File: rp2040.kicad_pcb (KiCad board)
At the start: 2 copper layers, 32 parts, among them J1 USB_C_Receptacle_USB2.0, J2 Conn_01x18, J3 Conn_01x18, SW1 SW_SPST, SW2 SW_SPST, U1 W25Q32JVSS, U2 AP1117-33, U3 RP2040, Y1 12MHz

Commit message: Routing finished
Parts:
- added J4: Conn_01x08, footprints:SOIC_clipProgSmall, F.Cu at (144.8, 104.5)
- added R8: 1K, Resistor_SMD:R_0402_1005Metric_Pad0.72x0.64mm_HandSolder, F.Cu at (168.9, 95.8)
- added kibuzzard-6203A46A: G***, kibuzzard-6203A46A, F.Cu at (178.1, 86.2)
- added kibuzzard-6203A47E: G***, kibuzzard-6203A47E, F.Cu at (178.1, 103.8)
- C1, C10, C11, C12, C13, C14, C15, C16, C4, C5, C6, C7, C8, C9: footprint Capacitor_SMD:C_0603_1608Metric_Pad1.08x0.95mm_HandSolder -> Capacitor_SMD:C_0402_1005Metric_Pad0.74x0.62mm_HandSolder
- C2, C3, U2: moved to B.Cu
- J2, J3: value Conn_01x18 -> Conn_02x10_Odd_Even; footprint Connector_PinHeader_2.54mm:PinHeader_1x18_P2.54mm_Vertical -> Connector_PinHeader_2.54mm:PinHeader_2x10_P2.54mm_Vertical
- R1, R2, R3, R4, R5, R6, R7: footprint Resistor_SMD:R_0603_1608Metric_Pad0.98x0.95mm_HandSolder -> Resistor_SMD:R_0402_1005Metric_Pad0.72x0.64mm_HandSolder
- U1: footprint Package_SO:SOIC-8_5.23x5.23mm_P1.27mm -> USON:SOIC-USON-8
- moved SW2 67.6 mm to (179.6, 108.5)
- moved R5 65.4 mm to (181.1, 105.5)
- moved C4 58.5 mm to (172.2, 99.0), turned to 180 degrees
- moved C13 56.1 mm to (164.3, 101.8), turned to -90 degrees
- moved C9 53.8 mm to (155.9, 95.7), turned to 180 degrees
- moved R7 53.4 mm to (156.6, 93.7), turned to 180 degrees
- moved R4 53.2 mm to (180.8, 89.3)
- moved U2 51.8 mm to (171.6, 89.5), turned to 180 degrees
- moved R6 51.8 mm to (156.6, 94.7), turned to 180 degrees
- moved C2 50.7 mm to (174.3, 94.0), turned to 180 degrees
- moved C11 50.7 mm to (159.8, 101.4), turned to -90 degrees
- moved C7 50.5 mm to (170.0, 92.5)
- moved Y1 50.3 mm to (172.2, 96.8), turned to 180 degrees
- moved C1 48.4 mm to (146.7, 89.4)
- moved R3 47.8 mm to (180.8, 101.2), turned to 180 degrees
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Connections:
- J2 pad 10: /GPIO8 -> /GPIO7
- J2 pad 11: /GPIO9 -> /GPIO8
- J2 pad 12: /GPIO10 -> /GPIO9
- J2 pad 13: /GPIO11 -> /GPIO10
- J2 pad 14: /GPIO12 -> /GPIO11
- J2 pad 15: /GPIO13 -> /GPIO12
- J2 pad 16: /GPIO14 -> +3V3
- J2 pad 17: /GPIO15 -> /GPIO13
- J2 pad 18: GND -> /GPIO14
- J2 pad 2: /GPIO0 -> /RUN
- J2 pad 3: /GPIO1 -> unconnected-(J2-Pad3)
- J2 pad 4: /GPIO2 -> unconnected-(J2-Pad4)
- J2 pad 5: /GPIO3 -> /GPIO2
- J2 pad 6: /GPIO4 -> /GPIO3
- J2 pad 7: /GPIO5 -> /GPIO4
- J2 pad 8: /GPIO6 -> /GPIO5
- J2 pad 9: /GPIO7 -> /GPIO6
- J3 pad 1: GND -> /GPIO0
- J3 pad 10: /GPIO22 -> /GPIO25
- J3 pad 11: /GPIO23 -> /GPIO22
- J3 pad 12: /GPIO24 -> /GPIO23
- J3 pad 13: /GPIO25 -> GND
- J3 pad 14: /GPIO26 -> /GPIO21
- J3 pad 15: /GPIO27 -> VBUS
- J3 pad 16: /GPIO28 -> /GPIO20
- J3 pad 17: /GPIO29 -> /GPIO18
- J3 pad 18: GND -> /GPIO19
- J3 pad 2: VBUS -> GND
- J3 pad 3: +3V3 -> /GPIO1
- J3 pad 4: /GPIO16 -> unconnected-(J3-Pad4)
- J3 pad 5: /GPIO17 -> /GPIO28
- J3 pad 6: /GPIO18 -> /GPIO29
- J3 pad 7: /GPIO19 -> /GPIO26
- J3 pad 8: /GPIO20 -> /GPIO27
- J3 pad 9: /GPIO21 -> /GPIO24
- R5 pad 2: Net-(R5-Pad2) -> /RUN
- SW2 pad 2: Net-(R5-Pad2) -> /RUN
- U3 pad 21: Net-(C5-Pad2) -> Net-(R8-Pad2)
- U3 pad 24: unconnected-(U3-Pad24) -> /SWCLK
- U3 pad 25: unconnected-(U3-Pad25) -> /SWD
- U3 pad 26: Net-(R5-Pad2) -> /RUN
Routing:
- net +3V3: track 0.00 -> 124.0 mm, vias 0 -> 8
- net /QSPI_SS: track 0.00 -> 71.0 mm, vias 0 -> 2
- net /RUN: track 0.00 -> 67.5 mm, vias 0 -> 2
- net /GPIO1: track 0.00 -> 41.8 mm, vias 0 -> 2
- net /USB_D+: track 0.00 -> 39.5 mm, vias 0 -> 2
- net /USB_D-: track 0.00 -> 37.7 mm, vias 0 -> 2
- net /GPIO0: track 0.00 -> 35.7 mm, vias 0 -> 2
- net /SWCLK: track 0.00 -> 29.2 mm, vias 0 -> 1
- net /SWD: track 0.00 -> 27.7 mm, vias 0 -> 1
- net VBUS: track 0.00 -> 25.4 mm, vias 0 -> 2
- net /QSPI_SD3: track 0.00 -> 23.2 mm
- net /QSPI_SCLK: track 0.00 -> 21.7 mm
- net +1V1: track 0.00 -> 21.2 mm
- net /QSPI_SDO: track 0.00 -> 20.4 mm
- net /QSPI_SD1: track 0.00 -> 18.1 mm
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- added copper zone on B.Cu, net GND
- added copper zone on F.Cu, net GND
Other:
- board outline added: 39 x 31 mm

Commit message: Some random tweaks
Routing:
- net /GPIO2: track 16.6 -> 16.0 mm
- net /GPIO4: track 14.5 -> 13.9 mm
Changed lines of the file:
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@@
   (segment (start 150.4 102) (end 152.45 102) (width 0.2) (layer "B.Cu") (net 13))
   (segment (start 161.15 100.35) (end 161.35 100.15) (width 0.2) (layer "B.Cu") (net 13))
-  (segment (start 161.801467 102.098533) (end 160.7 103.2) (width 0.2) (layer "F.Cu") (net 14))
-  (segment (start 156.25 103.2) (end 154.85 104.6) (width 0.2) (layer "F.Cu") (net 14))
+  (segment (start 156 104.6) (end 154.85 105.75) (width 0.2) (layer "F.Cu") (net 14))
+  (segment (start 161.802444 100.141843) (end 161.802445 100.191839) (width 0.2) (layer "F.Cu") (net 14))
+  (segment (start 161.802445 100.191839) (end 161.801467 100.192817) (width 0.2) (layer "F.Cu") (net 14))
   (segment (start 161.801467 100.19303) (end 161.801319 100.193178) (width 0.2) (layer "F.Cu") (net 14))
-  (segment (start 161.802445 100.191839) (end 161.801467 100.192817) (width 0.2) (layer "F.Cu") (net 14))
-  (segment (start 161.801467 100.192817) (end 161.801467 100.19303) (width 0.2) (layer "F.Cu") (net 14))
+  (segment (start 159.3 104.6) (end 156 104.6) (width 0.2) (layer "F.Cu") (net 14))
+  (segment (start 161.801319 100.193178) (end 161.801467 100.33795) (width 0.2) (layer "F.Cu") (net 14))
   (segment (start 161.9 98.6875) (end 161.849511 98.737989) (width 0.2) (layer "F.Cu") (net 14))
-  (segment (start 161.802444 100.141843) (end 161.802445 100.191839) (width 0.2) (layer "F.Cu") (net 14))
-  (segment (start 160.7 103.2) (end 156.25 103.2) (width 0.2) (layer "F.Cu") (net 14))
-  (segment (start 154.85 104.6) (end 154.85 107.86) (width 0.2) (layer "F.Cu") (net 14))
   (segment (start 161.801467 100.33795) (end 161.801467 102.098533) (width 0.2) (layer "F.Cu") (net 14))
-  (segment (start 161.801319 100.193178) (end 161.801467 100.33795) (width 0.2) (layer "F.Cu") (net 14))
   (segment (start 154.85 107.86) (end 156.215 109.225) (width 0.2) (layer "F.Cu") (net 14))
   (segment (start 161.849511 98.737989) (end 161.849511 100.094776) (width 0.2) (layer "F.Cu") (net 14))
+  (segment (start 154.85 105.75) (end 154.85 107.86) (width 0.2) (layer "F.Cu") (net 14))
+  (segment (start 161.801467 102.098533) (end 159.3 104.6) (width 0.2) (layer "F.Cu") (net 14))
+  (segment (start 161.801467 100.192817) (end 161.801467 100.19303) (width 0.2) (layer "F.Cu") (net 14))
   (segment (start 161.849511 100.094776) (end 161.802444 100.141843) (width 0.2) (layer "F.Cu") (net 14))
-  (segment (start 157.38 103.7) (end 156.215 104.865) (width 0.2) (layer "F.Cu") (net 15))
+  (segment (start 156.215 105.685) (end 156.215 106.685) (width 0.2) (layer "F.Cu") (net 15))
+  (segment (start 162.150978 102.249022) (end 159.45 104.95) (width 0.2) (layer "F.Cu") (net 15))
+  (segment (start 162.3 98.6875) (end 162.3 100.188571) (width 0.2) (layer "F.Cu") (net 15))
   (segment (start 162.3 100.188571) (end 162.150978 100.337593) (width 0.2) (layer "F.Cu") (net 15))
-  (segment (start 162.150978 102.249022) (end 160.7 103.7) (width 0.2) (layer "F.Cu") (net 15))
-  (segment (start 156.215 104.865) (end 156.215 106.685) (width 0.2) (layer "F.Cu") (net 15))
-  (segment (start 160.7 103.7) (end 157.38 103.7) (width 0.2) (layer "F.Cu") (net 15))
+  (segment (start 159.45 104.95) (end 156.95 104.95) (width 0.2) (layer "F.Cu") (net 15))
   (segment (start 162.150978 100.337593) (end 162.150978 102.249022) (width 0.2) (layer "F.Cu") (net 15))
-  (segment (start 162.3 98.6875) (end 162.3 100.188571) (width 0.2) (layer "F.Cu") (net 15))
-  (segment (start 157.655489 104.794511) (end 158.25 104.2) (width 0.2) (layer "F.Cu") (net 16))
-  (segment (start 162.649511 100.333343) (end 162.649511 99.717642) (width 0.2) (layer "F.Cu") (net 16))
-  (segment (start 162.649511 99.717642) (end 162.7 99.667153) (width 0.2) (layer "F.Cu") (net 16))
-  (segment (start 157.655489 108.125489) (end 157.655489 104.794511) (width 0.2) (layer "F.Cu") (net 16))
-  (segment (start 162.500489 100.482365) (end 162.649511 100.333343) (width 0.2) (layer "F.Cu") (net 16))
-  (segment (start 158.755 109.225) (end 157.655489 108.125489) (width 0.2) (layer "F.Cu") (net 16))
-  (segment (start 162.500489 102.449511) (end 162.500489 100.482365) (width 0.2) (layer "F.Cu") (net 16))
-  (segment (start 162.7 99.667153) (end 162.7 98.6875) (width 0.2) (layer "F.Cu") (net 16))
-  (segment (start 158.25 104.2) (end 160.75 104.2) (width 0.2) (layer "F.Cu") (net 16))
-  (segment (start 160.75 104.2) (end 162.500489 102.449511) (width 0.2) (layer "F.Cu") (net 16))
+  (segment (start 156.95 104.95) (end 156.215 105.685) (width 0.2) (layer "F.Cu") (net 15))
+  (segment (start 162.500489 100.482365) (end 162.500489 102.449511) (width 0.2) (layer "F.Cu") (net 16))
+  (segment (start 162.7 98.6875) (end 162.7 99.667153) (width 0.2) (layer "F.Cu") (net 16))
+  (segment (start 162.500489 102.449511) (end 159.65 105.3) (width 0.2) (layer "F.Cu") (net 16))
+  (segment (start 157.6 106) (end 157.6 108.07) (width 0.2) (layer "F.Cu") (net 16))
+  (segment (start 162.7 99.667153) (end 162.649511 99.717642) (width 0.2) (layer "F.Cu") (net 16))
+  (segment (start 158.3 105.3) (end 157.6 106) (width 0.2) (layer "F.Cu") (net 16))
+  (segment (start 159.65 105.3) (end 158.3 105.3) (width 0.2) (layer "F.Cu") (net 16))
+  (segment (start 162.649511 99.717642) (end 162.649511 100.333343) (width 0.2) (layer "F.Cu") (net 16))
+  (segment (start 162.649511 100.333343) (end 162.500489 100.482365) (width 0.2) (layer "F.Cu") (net 16))
+  (segment (start 157.6 108.07) (end 158.755 109.225) (width 0.2) (layer "F.Cu") (net 16))
   (segment (start 162.850978 102.699022) (end 162.850978 100.62616) (width 0.2) (layer "F.Cu") (net 17))
   (segment (start 158.755 106.685) (end 158.865 106.685) (width 0.2) (layer "F.Cu") (net 17))

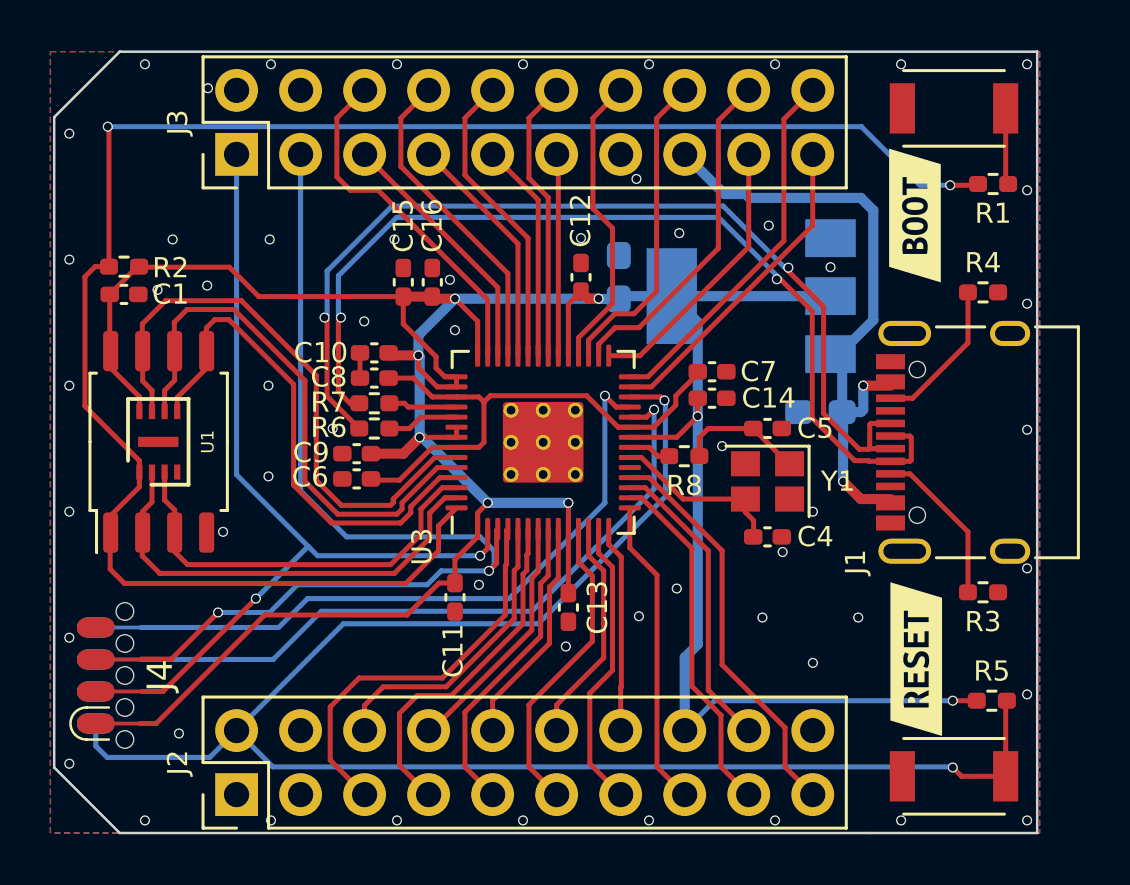
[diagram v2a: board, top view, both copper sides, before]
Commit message: Rearranged pinheaders, added logo and random tweaks
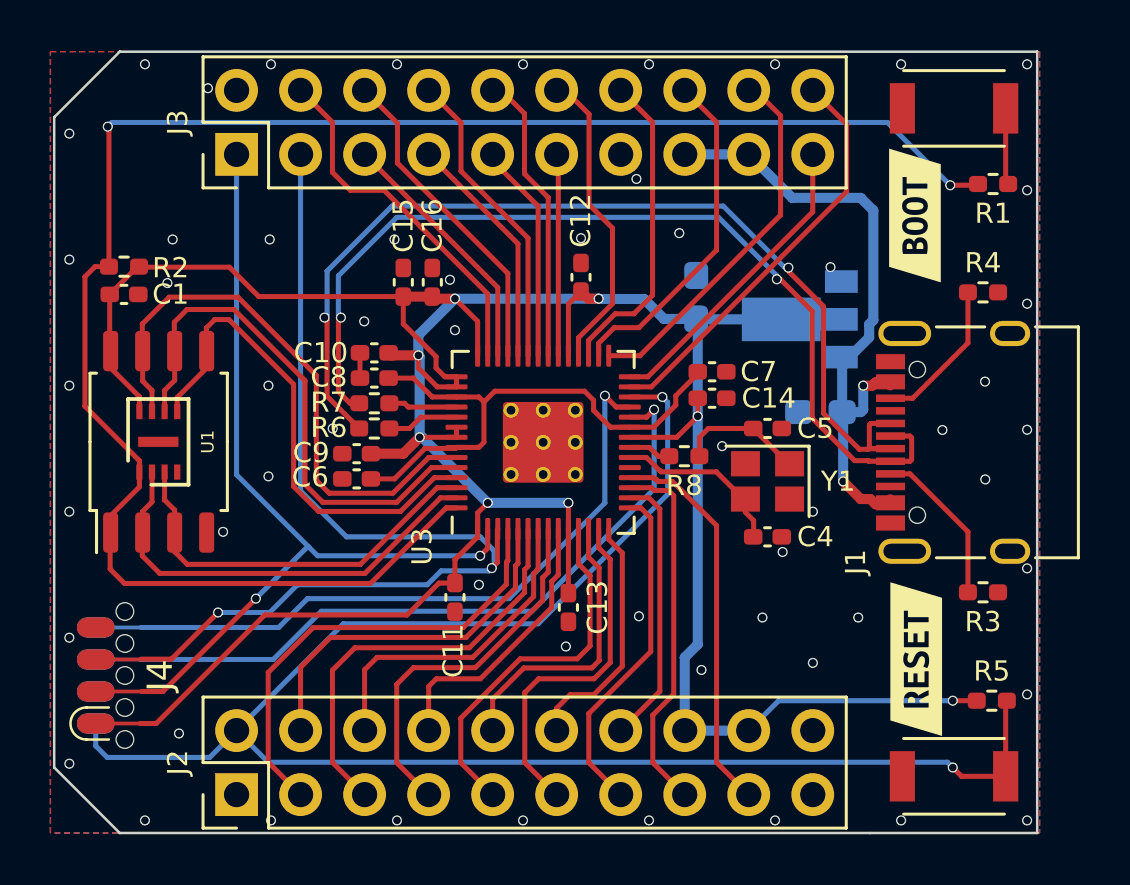
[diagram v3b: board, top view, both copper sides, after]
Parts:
- added G***: LOGO, LOGO, B.Cu at (154.1, 93.7)
- U2: footprint Package_TO_SOT_SMD:SOT-223-3_TabPin2 -> Package_TO_SOT_SMD:SOT-89-3
- moved C3 3.17 mm to (169.4, 89.5)
- moved U2 2.14 mm to (173.5, 90.4)
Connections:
- J2 pad 10: /GPIO7 -> /GPIO9
- J2 pad 11: /GPIO8 -> /GPIO10
- J2 pad 12: /GPIO9 -> /GPIO11
- J2 pad 13: /GPIO10 -> /GPIO12
- J2 pad 14: /GPIO11 -> /GPIO13
- J2 pad 15: /GPIO12 -> /GPIO14
- J2 pad 17: /GPIO13 -> /GPIO15
- J2 pad 18: /GPIO14 -> +3V3
- J2 pad 19: /GPIO15 -> GND
- J2 pad 20: unconnected-(J2-Pad20) -> GND
- J2 pad 3: unconnected-(J2-Pad3) -> /GPIO2
- J2 pad 4: unconnected-(J2-Pad4) -> /GPIO3
- J2 pad 5: /GPIO2 -> /GPIO4
- J2 pad 6: /GPIO3 -> /GPIO5
- J2 pad 7: /GPIO4 -> /GPIO6
- J2 pad 8: /GPIO5 -> /GPIO7
- J2 pad 9: /GPIO6 -> /GPIO8
- J3 pad 10: /GPIO25 -> /GPIO23
- J3 pad 12: /GPIO23 -> /GPIO21
- J3 pad 14: /GPIO21 -> /GPIO20
- J3 pad 16: /GPIO20 -> /GPIO19
- J3 pad 17: /GPIO18 -> VBUS
- J3 pad 18: /GPIO19 -> /GPIO18
- J3 pad 19: /GPIO16 -> /GPIO17
- J3 pad 20: /GPIO17 -> /GPIO16
- J3 pad 4: unconnected-(J3-Pad4) -> /GPIO29
- J3 pad 6: /GPIO29 -> /GPIO27
- J3 pad 8: /GPIO27 -> /GPIO25
- U1 pad 9: (no net) -> GND
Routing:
- net /GPIO18: track 11.0 -> 14.8 mm
- net /GPIO16: track 12.7 -> 16.4 mm
- net /GPIO5: track 9.86 -> 13.1 mm
- net /GPIO13: track 14.0 -> 10.8 mm
- net /GPIO4: track 13.9 -> 16.9 mm
- net /GPIO3: track 12.0 -> 14.7 mm
- net /GPIO14: track 11.9 -> 14.6 mm
- net /GPIO6: track 12.4 -> 15.0 mm
- net /GPIO17: track 14.8 -> 12.2 mm
- net /GPIO2: track 16.0 -> 18.5 mm
- net /GPIO9: track 9.02 -> 11.5 mm
- net /GPIO8: track 12.3 -> 14.7 mm
- net /GPIO10: track 11.6 -> 13.9 mm
- net /GPIO7: track 9.08 -> 11.2 mm
- net /GPIO11: track 8.21 -> 9.85 mm
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
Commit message: Final touches for the manufacturing process
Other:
- board text added: "JLCJLCJLCJLC"
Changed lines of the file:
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@@
       (usegerberattributes true)
       (usegerberadvancedattributes true)
-      (creategerberjobfile true)
+      (creategerberjobfile false)
       (svguseinch false)
       (svgprecision 6)
@@
     (property "Sheetname" "")
     (attr smd)
-    (fp_text reference "U3" (at -4.136575 -4.801255 90) (layer "F.SilkS")
+    (fp_text reference "U3" (at -3.43 -5.21 180) (layer "F.SilkS")
       (effects (font (size 0.8 0.8) (thickness 0.15)))
     )
@@
     (property "Sheetname" "")
     (attr smd)
-    (fp_text reference "C12" (at 2.25 -0.006137 90) (layer "F.SilkS")
+    (fp_text reference "C12" (at -0.01 -1.11 90) (layer "F.SilkS")
       (effects (font (size 0.8 0.8) (thickness 0.15)))
     )
@@
     (property "Sheetname" "")
     (attr smd)
-    (fp_text reference "C11" (at 2.12132 0.070711 90) (layer "F.SilkS")
+    (fp_text reference "C11" (at 0.01 -1.1 90) (layer "F.SilkS")
       (effects (font (size 0.8 0.8) (thickness 0.15)))
     )
@@
     (property "Sheetname" "")
     (attr smd)
-    (fp_text reference "J1" (at -4.75 -5.05 90) (layer "F.SilkS")
+    (fp_text reference "J1" (at -5.15 -5.16 180) (layer "F.SilkS")
       (effects (font (size 0.8 0.8) (thickness 0.15)))
     )
@@
     (attr smd)
     (fp_text reference "U1" (at 1.96 0 90) (layer "F.SilkS")
-      (effects (font (size 0.5 0.5) (thickness 0.125)))
+      (effects (font (size 0.8 0.8) (thickness 0.125)))
     )
     (fp_text value "W25Q32JVSS" (at 2.7232 0.035 90) (layer "F.Fab") hide
@@
     )
     (fp_text user "${REFERENCE}" (at 0.015 0 90) (layer "F.Fab")
-      (effects (font (size 1 1) (thickness 0.15)))
+      (effects (font (size 0.8 0.8) (thickness 0.15)))
     )
     (fp_line (start 2.74 -2.725) (end 2.48 -2.725) (layer "F.SilkS") (width 0.12))
@@
     (attr through_hole)
     (fp_text reference "J4" (at 0 -3.302 90) (layer "F.SilkS")
-      (effects (font (size 1 1) (thickness 0.15)))
+      (effects (font (size 0.8 0.8) (thickness 0.15)))
     )
     (fp_text value "Conn_01x08" (at 0.127 1.397 90) (layer "F.Fab")
@@
     (attr board_only exclude_from_pos_files exclude_from_bom)
     (fp_text reference "kibuzzard-6203A47E" (at 0 -1.025901 90) (layer "F.SilkS") hide
-      (effects (font (size 0.000254 0.000254) (thickness 0.000003)))
+      (effects (font (size 0.8 0.8) (thickness 0.000003)))
     )
     (fp_text value "G***" (at 0 1.025901 90) (layer "F.SilkS") hide
@@
     (property "Sheetname" "")
     (attr smd)
-    (fp_text reference "C16" (at 2.25 0 90) (layer "F.SilkS")
+    (fp_text reference "C16" (at 0 1.27 90) (layer "F.SilkS")
       (effects (font (size 0.8 0.8) (thickness 0.15)))
     )
@@
     (property "Sheetname" "")
     (attr smd)
-    (fp_text reference "C15" (at 2.25 0 90) (layer "F.SilkS")
+    (fp_text reference "C15" (at -0.01 -1.03 90) (layer "F.SilkS")
       (effects (font (size 0.8 0.8) (thickness 0.15)))
     )
@@
     (attr board_only exclude_from_pos_files exclude_from_bom)
     (fp_text reference "kibuzzard-6203A46A" (at 0 -1.025901 90) (layer "F.SilkS") hide
-      (effects (font (size 0.000254 0.000254) (thickness 0.000003)))
+      (effects (font (size 0.8 0.8) (thickness 0.000003)))
     )
     (fp_text value "G***" (at 0 1.025901 90) (layer "F.SilkS") hide
@@
     (property "Sheetname" "")
     (attr smd)
-    (fp_text reference "C3" (at 2.5 0 90) (layer "B.SilkS")
+    (fp_text reference "C3" (at -0.0075 -1.33 90) (layer "B.SilkS")
       (effects (font (size 0.8 0.8) (thickness 0.15)) (justify mirror))
     )
@@
     (property "Sheetname" "")
     (attr smd)
-    (fp_text reference "C2" (at 2.25 0) (layer "B.SilkS")
+    (fp_text reference "C2" (at 0.01 -1.54) (layer "B.SilkS")
       (effects (font (size 0.8 0.8) (thickness 0.15)) (justify mirror))
     )
@@
     (attr smd)
     (fp_text reference "U2" (at 0.3 3.5) (layer "B.SilkS")
-      (effects (font (size 1 1) (thickness 0.15)) (justify mirror))
+      (effects (font (size 0.8 0.8) (thickness 0.15)) (justify mirror))
     )
     (fp_text value "AP1117-33" (at 0.3 -3.5) (layer "B.Fab")
@@
     )
     (fp_text user "${REFERENCE}" (at 0.5 0 90) (layer "B.Fab")
-      (effects (font (size 1 1) (thickness 0.15)) (justify mirror))
+      (effects (font (size 0.8 0.8) (thickness 0.15)) (justify mirror))
     )
     (fp_line (start 1.66 -1.05) (end 1.66 -2.36) (layer "B.SilkS") (width 0.12))
@@
       (primitives
         (gr_poly (pts
+            (xy 3.8625 0.8665)
+            (xy 0.7375 0.8665)
+            (xy 0.7375 -0.8665)
             (xy 3.8625 -0.8665)
-            (xy 0.7375 -0.8665)
-            (xy 0.7375 0.8665)
-            (xy 3.8625 0.8665)
           ) (width 0) (fill yes))
       ))
@@
     (attr board_only exclude_from_pos_files exclude_from_bom)
     (fp_text reference "G***" (at 0 0 90) (layer "B.SilkS") hide
-      (effects (font (size 1.524 1.524) (thickness 0.3)) (justify mirror))
+      (effects (font (size 0.8 0.8) (thickness 0.3)) (justify mirror))
     )
     (fp_text value "LOGO" (at 0.75 0 90) (layer "B.SilkS") hide
@@
   (gr_line (start 143.9 108.15) (end 143.9 82.35) (layer "Edge.Cuts") (width 0.1))
   (gr_line (start 146.5 79.75) (end 182.9 79.75) (layer "Edge.Cuts") (width 0.1))
+  (gr_text "JLCJLCJLCJLC" (at 179.94 95.25 90) (layer "F.SilkS")
+    (effects (font (size 0.8 0.8) (thickness 0.2)))
+  )
   (dimension (type aligned) (layer "Dwgs.User")
     (pts (xy 195.29 109.19) (xy 195.29 81.25))
